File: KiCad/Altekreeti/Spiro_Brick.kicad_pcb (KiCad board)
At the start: 2 copper layers, 70 x 70 mm, 32 parts, among them J1 JST_SMD_1.0mm_Vertical, J3 Conn_01x09_Pin, J4 JST_SMD_1.0mm_Vertical, Q1 MMUN2133LT1G, Q2 BSS138, Q3 BSS138, U1 TPS61090, U2 Amphenol_8DIP_Code_1, U3 Amphenol_8DIP_Code_1

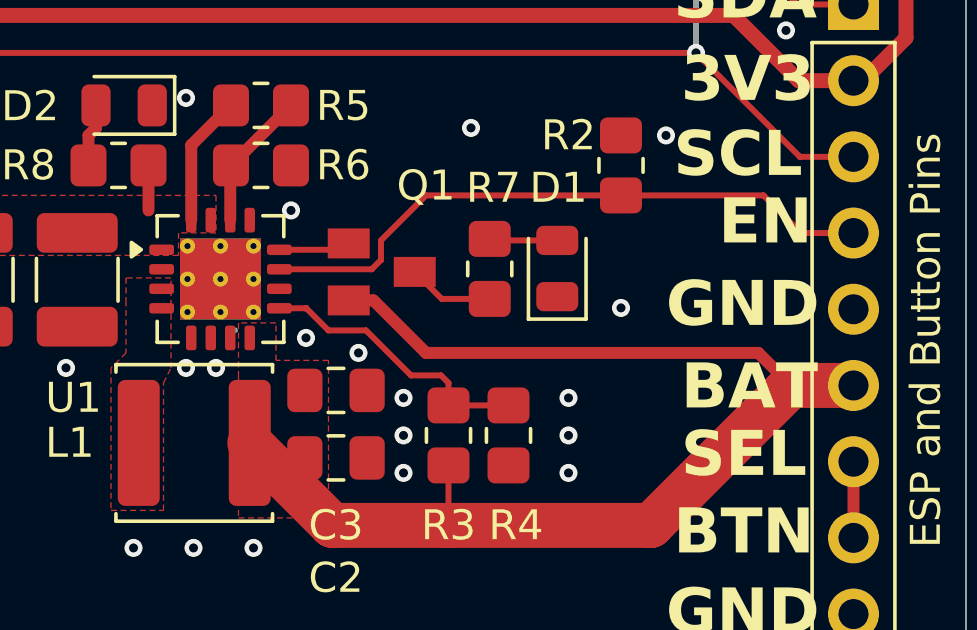
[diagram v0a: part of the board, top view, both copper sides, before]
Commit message: Fix inductor ground loop
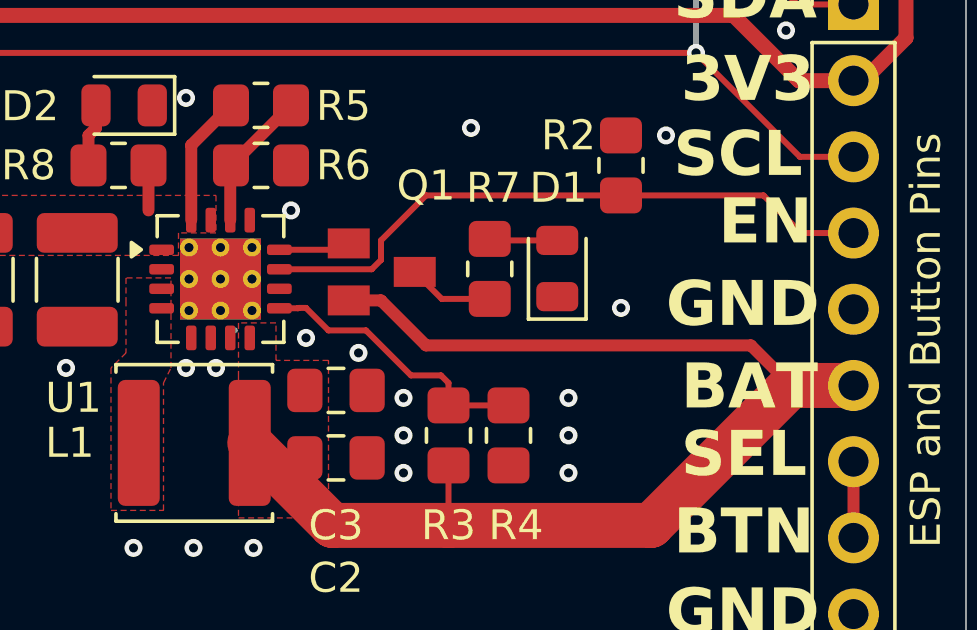
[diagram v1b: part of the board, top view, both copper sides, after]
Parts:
- U1: footprint Package_DFN_QFN:Texas_RSA_VQFN-16-1EP_4x4mm_P0.65mm_EP2.7x2.7mm_ThermalVias -> Spiro_Brick:Texas_RSA_VQFN-16-1EP_4x4mm_P0.65mm_EP2.7x2.7mm_ThermalVias
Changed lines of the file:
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@@
 		)
 		(property "Value" "6.8uH"
-			(at -4.85 0 0)
+			(at 5.275 -1.5 0)
 			(layer "F.Fab")
 			(effects
@@
 		)
 		(fp_text user "${REFERENCE}"
-			(at 0 0 0)
+			(at -0.225 0.25 0)
 			(layer "F.Fab")
 			(effects
@@
 		)
 		(property "Value" "10uF"
-			(at 0 0 0)
+			(at 2.75 4.5 0)
 			(layer "F.Fab")
 			(effects
@@
 		)
 	)
-	(footprint "Package_DFN_QFN:Texas_RSA_VQFN-16-1EP_4x4mm_P0.65mm_EP2.7x2.7mm_ThermalVias"
+	(footprint "Spiro_Brick:Texas_RSA_VQFN-16-1EP_4x4mm_P0.65mm_EP2.7x2.7mm_ThermalVias"
 		(layer "F.Cu")
 		(at 65.15 79.5375)
@@
 		)
 		(property "Value" "TPS61090"
-			(at -0.025 1.2125 0)
+			(at 0 3.33 0)
 			(layer "F.Fab")
 			(effects
@@
 			)
 		)
-		(property "Datasheet" "http://www.ti.com/lit/ds/symlink/tps61090.pdf"
+		(property "Datasheet" ""
 			(at 0 0 0)
 			(layer "F.Fab")
@@
 			)
 		)
-		(property "Description" "2A Step-Up DC-DC Converter for Batteries, Isw up to 2500mA, Adjustable output voltage, QFN-16"
+		(property "Description" ""
 			(at 0 0 0)
 			(layer "F.Fab")
@@
 		)
 		(pad "17" thru_hole circle
-			(at -1.1 -1.1)
-			(size 0.5 0.5)
-			(drill 0.2)
+			(at -1.05 -1.05)
+			(size 0.6 0.6)
+			(drill 0.3)
 			(property pad_prop_heatsink)
 			(layers "*.Cu")
@@
 		)
 		(pad "17" thru_hole circle
-			(at -1.1 0)
-			(size 0.5 0.5)
-			(drill 0.2)
+			(at -1.05 0)
+			(size 0.6 0.6)
+			(drill 0.3)
 			(property pad_prop_heatsink)
 			(layers "*.Cu")
@@
 		)
 		(pad "17" thru_hole circle
-			(at -1.1 1.1)
-			(size 0.5 0.5)
-			(drill 0.2)
+			(at -1.05 1.05)
+			(size 0.6 0.6)
+			(drill 0.3)
 			(property pad_prop_heatsink)
 			(layers "*.Cu")
@@
 		)
 		(pad "17" thru_hole circle
-			(at 0 -1.1)
-			(size 0.5 0.5)
-			(drill 0.2)
+			(at 0 -1.05)
+			(size 0.6 0.6)
+			(drill 0.3)
 			(property pad_prop_heatsink)
 			(layers "*.Cu")
@@
 		(pad "17" thru_hole circle
 			(at 0 0)
-			(size 0.5 0.5)
-			(drill 0.2)
+			(size 0.6 0.6)
+			(drill 0.3)
 			(property pad_prop_heatsink)
 			(layers "*.Cu")
@@
 		)
 		(pad "17" thru_hole circle
-			(at 0 1.1)
-			(size 0.5 0.5)
-			(drill 0.2)
+			(at 0 1.05)
+			(size 0.6 0.6)
+			(drill 0.3)
 			(property pad_prop_heatsink)
 			(layers "*.Cu")
@@
 		)
 		(pad "17" thru_hole circle
-			(at 1.1 -1.1)
-			(size 0.5 0.5)
-			(drill 0.2)
+			(at 1.05 -1.05)
+			(size 0.6 0.6)
+			(drill 0.3)
 			(property pad_prop_heatsink)
 			(layers "*.Cu")
@@
 		)
 		(pad "17" thru_hole circle
-			(at 1.1 0)
-			(size 0.5 0.5)
-			(drill 0.2)
+			(at 1.05 0)
+			(size 0.6 0.6)
+			(drill 0.3)
 			(property pad_prop_heatsink)
 			(layers "*.Cu")
@@
 		)
 		(pad "17" thru_hole circle
-			(at 1.1 1.1)
-			(size 0.5 0.5)
-			(drill 0.2)
+			(at 1.05 1.05)
+			(size 0.6 0.6)
+			(drill 0.3)
 			(property pad_prop_heatsink)
 			(layers "*.Cu")
@@
 		)
 		(property "Value" "0.1uF"
-			(at -3.375 0 0)
+			(at -1 5.5 0)
 			(layer "F.Fab")
 			(effects
@@
 	)
 	(segment
-		(start 70.25 80.25)
-		(end 72 82)
+		(start 72 81.75)
+		(end 82.83 81.75)
 		(width 0.4)
 		(layer "F.Cu")
@@
 	)
 	(segment
-		(start 83.08 82)
-		(end 84.165 83.085)
-		(width 0.4)
+		(start 72.75 87.75)
+		(end 68.875 87.75)
+		(width 1.5)
 		(layer "F.Cu")
 		(net 3)
@@
 	(segment
 		(start 69.425 80.25)
-		(end 70.25 80.25)
+		(end 70.5 80.25)
 		(width 0.4)
 		(layer "F.Cu")
@@
 	)
 	(segment
-		(start 72.75 87.75)
-		(end 68.875 87.75)
-		(width 1.5)
+		(start 70.5 80.25)
+		(end 72 81.75)
+		(width 0.4)
 		(layer "F.Cu")
 		(net 3)
 	)
 	(segment
-		(start 72 82)
-		(end 83.08 82)
+		(start 82.83 81.75)
+		(end 84.165 83.085)
 		(width 0.4)
 		(layer "F.Cu")
@@
 	)
 	(segment
-		(start 67.9875 80.5125)
-		(end 68 80.5)
-		(width 0.2)
-		(layer "F.Cu")
-		(net 10)
-	)
-	(segment
 		(start 70 81.25)
 		(end 71.5 82.75)
@@
 	)
 	(segment
-		(start 67.1125 80.5125)
-		(end 67.9875 80.5125)
+		(start 68 80.5)
+		(end 68.75 81.25)
 		(width 0.2)
 		(layer "F.Cu")
@@
 	)
 	(segment
-		(start 68 80.5)
-		(end 68.75 81.25)
+		(start 67.75 80.5)
+		(end 67.7375 80.5125)
 		(width 0.2)
 		(layer "F.Cu")
@@
 	)
 	(segment
+		(start 67.7375 80.5125)
+		(end 67.1125 80.5125)
+		(width 0.2)
+		(layer "F.Cu")
+		(net 10)
+	)
+	(segment
 		(start 72.75 83)
 		(end 72.75 83.75)
@@
 	)
 	(segment
+		(start 68 80.5)
+		(end 67.75 80.5)
+		(width 0.2)
+		(layer "F.Cu")
+		(net 10)
+	)
+	(segment
 		(start 67.5 73.75)
 		(end 65.5 75.75)
@@
 			)
 		)
+	)
+	(zone
+		(net 0)
+		(net_name "")
+		(layers "F.Cu" "B.Cu")
+		(hatch edge 0.5)
+		(connect_pads
+			(clearance 0)
+		)
+		(min_thickness 0.25)
+		(filled_areas_thickness no)
+		(keepout
+			(tracks not_allowed)
+			(vias not_allowed)
+			(pads not_allowed)
+			(copperpour not_allowed)
+			(footprints allowed)
+		)
+		(placement
+			(enabled no)
+			(sheetname "")
+		)
+		(fill
+			(thermal_gap 0.5)
+			(thermal_bridge_width 0.5)
+		)
+		(polygon
+			(pts
+				(xy 63.5 83) (xy 65.25 83) (xy 65.25 87.25) (xy 63.5 87.25)
+			)
+		)
